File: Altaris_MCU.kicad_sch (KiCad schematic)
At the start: 81 parts, among them J1 Screw_Terminal_01x02, J10 USB_C_Receptacle_USB2.0_16P, J11 Screw_Terminal_01x02, J2 Screw_Terminal_01x02, J3 Screw_Terminal_01x02, J4 Screw_Terminal_01x02, J5 Screw_Terminal_01x02, J6 Screw_Terminal_01x02, J7 Conn_01x08_Socket, J8 Screw_Terminal_01x02, J9 USB_C_Receptacle_USB2.0_16P, Q1 Q_NMOS, SW2 RESET1, SW3 BOOT1, U1 ESP32-S3-WROOM-1, U10 USBLC6-2SC6, U11 MAX31855KASA, U12 TPS62827DMQT, U13 USBLC6-2SC6, U15 CH340X, U2 MAX31855KASA, U3 TPS79333-EP, U4 ICM-20948, U5 TPS79318-EP, U6 SN74AVC4T774RSVR, U7 MAX31855KASA, U8 MAX31855KASA, U9 SN74AVC4T774RSVR

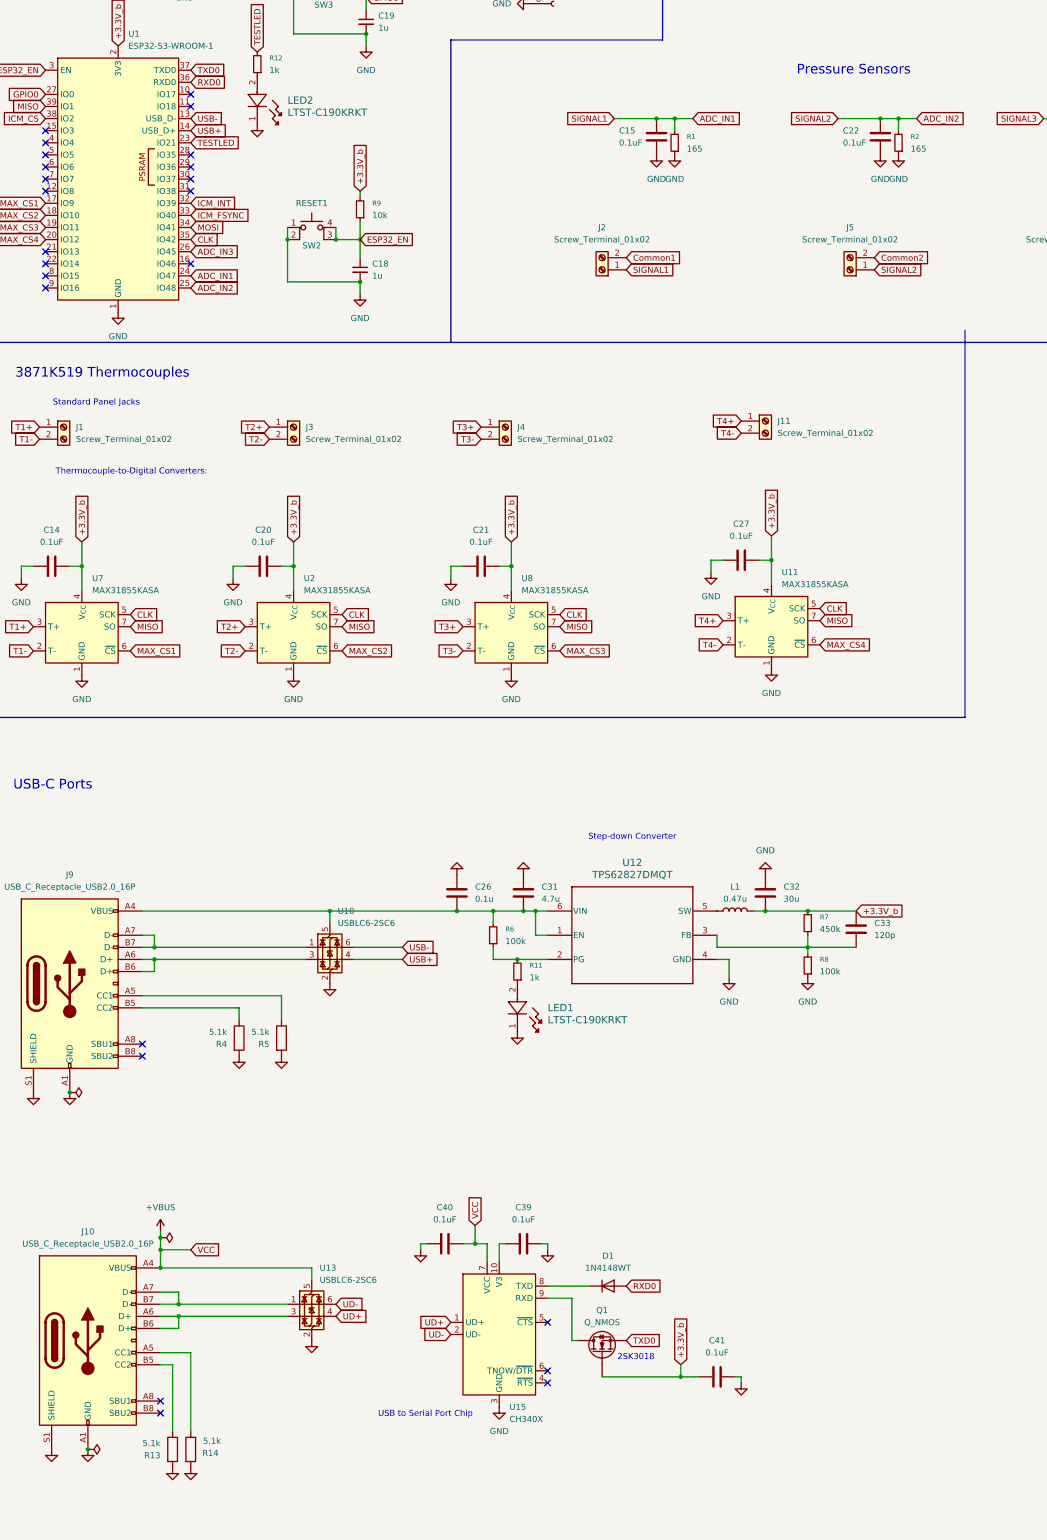
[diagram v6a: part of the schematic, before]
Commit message: Small changes to USB ports, ran ERC
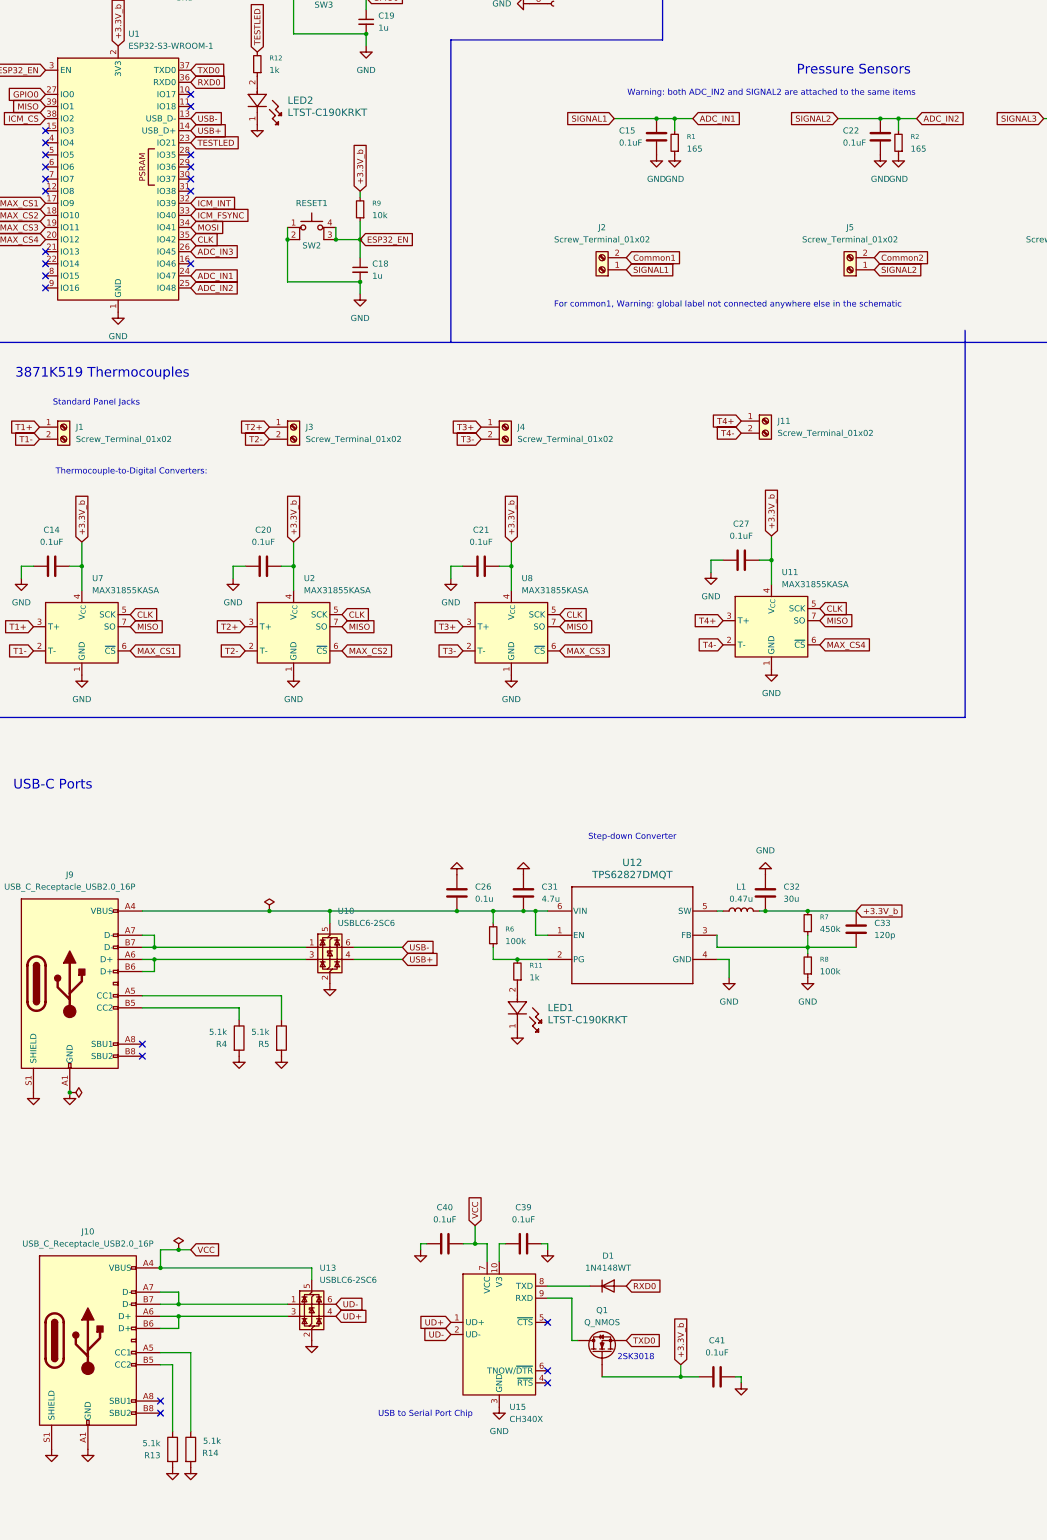
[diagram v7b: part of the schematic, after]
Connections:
- net +VBUS renamed VCC
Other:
- note added: "For common1, Warning: global label not connected anywhere else in the schematic"
- note added: "Warning: both ADC_IN2 and SIGNAL2 are attached to the same items"
- moved on the sheet: L1
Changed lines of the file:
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@@
 		)
 	)
+	(text "For common1, Warning: global label not connected anywhere else in the schematic"
+		(exclude_from_sim no)
+		(at 169.926 106.426 0)
+		(effects
+			(font
+				(size 1.27 1.27)
+			)
+		)
+	)
 	(text "Step-down Converter"
 		(exclude_from_sim no)
@@
 		)
 	)
+	(text "Warning: both ADC_IN2 and SIGNAL2 are attached to the same items"
+		(exclude_from_sim no)
+		(at 179.07 61.976 0)
+		(effects
+			(font
+				(size 1.27 1.27)
+			)
+		)
+	)
 	(text "WILL PROBOLY GET RID OF THIS LDO\n					   	    "
 		(exclude_from_sim no)
@@
 	)
 	(junction
-		(at 35.56 346.71)
-		(diameter 0)
-		(color 0 0 0 0)
-	)
-	(junction
 		(at 78.74 41.91)
 		(diameter 0)
@@
 	)
 	(junction
+		(at 73.66 233.68)
+		(diameter 0)
+		(color 0 0 0 0)
+	)
+	(junction
 		(at 120.65 233.68)
 		(diameter 0)
@@
 	)
 	(junction
+		(at 54.61 304.8)
+		(diameter 0)
+		(color 0 0 0 0)
+	)
+	(junction
 		(at 542.29 140.97)
 		(diameter 0)
@@
 	)
 	(junction
-		(at 50.8 302.26)
-		(diameter 0)
-		(color 0 0 0 0)
-	)
-	(junction
 		(at 350.52 44.45)
 		(diameter 0)
@@
 	)
 	(junction
-		(at 50.8 304.8)
-		(diameter 0)
-		(color 0 0 0 0)
-	)
-	(junction
 		(at 186.69 233.68)
 		(diameter 0)
@@
 	(wire
 		(pts
-			(xy 50.8 302.26) (xy 50.8 304.8)
-		)
-		(stroke
-			(width 0)
-			(type default)
-		)
-	)
-	(wire
-		(pts
 			(xy 176.53 160.02) (xy 179.07 160.02)
 		)
@@
 	(wire
 		(pts
+			(xy 54.61 304.8) (xy 50.8 304.8)
+		)
+		(stroke
+			(width 0)
+			(type default)
+		)
+	)
+	(wire
+		(pts
 			(xy 170.18 243.84) (xy 170.18 247.65)
 		)
@@
 	(wire
 		(pts
+			(xy 168.91 233.68) (xy 167.64 233.68)
+		)
+		(stroke
+			(width 0)
+			(type default)
+		)
+	)
+	(wire
+		(pts
 			(xy 120.65 233.68) (xy 127 233.68)
 		)
@@
 	(wire
 		(pts
-			(xy 50.8 300.99) (xy 50.8 302.26)
-		)
-		(stroke
-			(width 0)
-			(type default)
-		)
-	)
-	(wire
-		(pts
 			(xy 474.98 114.3) (xy 474.98 130.81)
 		)
@@
 	(wire
 		(pts
-			(xy 46.99 233.68) (xy 86.36 233.68)
+			(xy 46.99 233.68) (xy 73.66 233.68)
 		)
 		(stroke
@@
 	(wire
 		(pts
-			(xy 57.15 304.8) (xy 50.8 304.8)
+			(xy 57.15 304.8) (xy 54.61 304.8)
 		)
 		(stroke
@@
 	(wire
 		(pts
+			(xy 73.66 233.68) (xy 86.36 233.68)
+		)
+		(stroke
+			(width 0)
+			(type default)
+		)
+	)
+	(wire
+		(pts
 			(xy 236.22 67.31) (xy 245.11 67.31)
 		)
@@
 	(wire
 		(pts
-			(xy 175.26 233.68) (xy 177.8 233.68)
+			(xy 176.53 233.68) (xy 177.8 233.68)
 		)
 		(stroke
@@
 	(symbol
 		(lib_id "power:PWR_FLAG")
-		(at 50.8 302.26 270)
+		(at 54.61 304.8 0)
 		(unit 1)
 		(exclude_from_sim no)
@@
 		(fields_autoplaced yes)
 		(property "Reference" "#FLG07"
-			(at 52.705 302.26 0)
+			(at 54.61 302.895 0)
 			(effects
 				(font
@@
 		)
 		(property "Value" "PWR_FLAG"
-			(at 55.88 302.26 0)
+			(at 54.61 299.72 0)
 			(effects
 				(font
@@
 		)
 		(property "Footprint" ""
-			(at 50.8 302.26 0)
+			(at 54.61 304.8 0)
 			(effects
 				(font
@@
 		)
 		(property "Datasheet" "~"
-			(at 50.8 302.26 0)
+			(at 54.61 304.8 0)
 			(effects
 				(font
@@
 		)
 		(property "Description" "Special symbol for telling ERC where power comes from"
-			(at 50.8 302.26 0)
+			(at 54.61 304.8 0)
 			(effects
 				(font
@@
 	)
 	(symbol
+		(lib_id "power:PWR_FLAG")
+		(at 73.66 233.68 0)
+		(unit 1)
+		(exclude_from_sim no)
+		(in_bom yes)
+		(on_board yes)
+		(dnp no)
+		(fields_autoplaced yes)
+		(property "Reference" "#FLG02"
+			(at 73.66 231.775 0)
+			(effects
+				(font
+					(size 1.27 1.27)
+				)
+				(hide yes)
+			)
+		)
+		(property "Value" "PWR_FLAG"
+			(at 73.66 228.6 0)
+			(effects
+				(font
+					(size 1.27 1.27)
+				)
+				(hide yes)
+			)
+		)
+		(property "Footprint" ""
+			(at 73.66 233.68 0)
+			(effects
+				(font
+					(size 1.27 1.27)
+				)
+				(hide yes)
+			)
+		)
+		(property "Datasheet" "~"
+			(at 73.66 233.68 0)
+			(effects
+				(font
+					(size 1.27 1.27)
+				)
+				(hide yes)
+			)
+		)
+		(property "Description" "Special symbol for telling ERC where power comes from"
+			(at 73.66 233.68 0)
+			(effects
+				(font
+					(size 1.27 1.27)
+				)
+				(hide yes)
+			)
+		)
+		(pin "1"
+		)
+		(instances
+			(project "Altaris_MCU"
+				(path "/21889916-6808-460c-a148-21d1f170ea7e"
+					(reference "#FLG02")
+					(unit 1)
+				)
+			)
+		)
+	)
+	(symbol
 		(lib_id "power:GND")
 		(at 518.16 71.12 270)
@@
 	)
 	(symbol
-		(lib_id "power:PWR_FLAG")
-		(at 35.56 346.71 270)
-		(unit 1)
-		(exclude_from_sim no)
-		(in_bom yes)
-		(on_board yes)
-		(dnp no)
-		(fields_autoplaced yes)
-		(property "Reference" "#FLG01"
-			(at 37.465 346.71 0)
-			(effects
-				(font
-					(size 1.27 1.27)
-				)
-				(hide yes)
-			)
-		)
-		(property "Value" "PWR_FLAG"
-			(at 40.64 346.71 0)
-			(effects
-				(font
-					(size 1.27 1.27)
-				)
-				(hide yes)
-			)
-		)
-		(property "Footprint" ""
-			(at 35.56 346.71 0)
-			(effects
-				(font
-					(size 1.27 1.27)
-				)
-				(hide yes)
-			)
-		)
-		(property "Datasheet" "~"
-			(at 35.56 346.71 0)
-			(effects
-				(font
-					(size 1.27 1.27)
-				)
-				(hide yes)
-			)
-		)
-		(property "Description" "Special symbol for telling ERC where power comes from"
-			(at 35.56 346.71 0)
-			(effects
-				(font
-					(size 1.27 1.27)
-				)
-				(hide yes)
-			)
-		)
-		(pin "1"
-		)
-		(instances
-			(project "Altaris_MCU"
-				(path "/21889916-6808-460c-a148-21d1f170ea7e"
-					(reference "#FLG01")
-					(unit 1)
-				)
-			)
-		)
-	)
-	(symbol
 		(lib_id "power:GND")
 		(at 377.19 36.83 180)
@@
 	)
 	(symbol
-		(lib_id "power:VBUS")
-		(at 50.8 300.99 0)
-		(unit 1)
-		(exclude_from_sim no)
-		(in_bom yes)
-		(on_board yes)
-		(dnp no)
-		(fields_autoplaced yes)
-		(property "Reference" "#PWR077"
-			(at 50.8 304.8 0)
-			(effects
-				(font
-					(size 1.27 1.27)
-				)
-				(hide yes)
-			)
-		)
-		(property "Value" "+VBUS"
-			(at 50.8 295.91 0)
-			(effects
-				(font
-					(size 1.27 1.27)
-				)
-			)
-		)
-		(property "Footprint" ""
-			(at 50.8 300.99 0)
-			(effects
-				(font
-					(size 1.27 1.27)
-				)
-				(hide yes)
-			)
-		)
-		(property "Datasheet" ""
-			(at 50.8 300.99 0)
-			(effects
-				(font
-					(size 1.27 1.27)
-				)
-				(hide yes)
-			)
-		)
-		(property "Description" "Power symbol creates a global label with name \"VBUS\""
-			(at 50.8 300.99 0)
-			(effects
-				(font
-					(size 1.27 1.27)
-				)
-				(hide yes)
-			)
-		)
-		(pin "1"
-		)
-		(instances
-			(project "Altaris_MCU"
-				(path "/21889916-6808-460c-a148-21d1f170ea7e"
-					(reference "#PWR077")
-					(unit 1)
-				)
-			)
-		)
-	)
-	(symbol
 		(lib_id "power:GND")
 		(at 111.76 163.83 0)
@@
 	(symbol
 		(lib_id "Device:L")
-		(at 171.45 233.68 90)
+		(at 172.72 233.68 90)
 		(unit 1)
 		(exclude_from_sim no)
@@
 		(fields_autoplaced yes)
 		(property "Reference" "L1"
-			(at 171.45 228.6 90)
+			(at 172.72 228.6 90)
 			(effects
 				(font
@@
 		)
 		(property "Value" "0.47u"
-			(at 171.45 231.14 90)
+			(at 172.72 231.14 90)
 			(effects
 				(font
@@
 		)
 		(property "Footprint" "MyFootprints:IND_XFL4015_COC"
-			(at 171.45 233.68 0)
+			(at 172.72 233.68 0)
 			(effects
 				(font
@@
 		)
 		(property "Datasheet" "~"
-			(at 171.45 233.68 0)
+			(at 172.72 233.68 0)
 			(effects
 				(font
@@
 		)
 		(property "Description" "Inductor"
-			(at 171.45 233.68 0)
+			(at 172.72 233.68 0)
 			(effects
 				(font

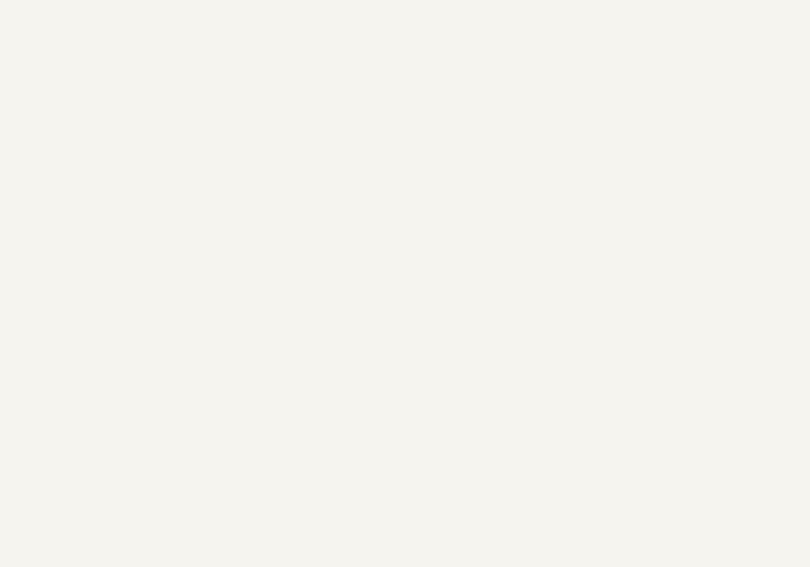
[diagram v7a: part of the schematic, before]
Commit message: added stitching vias, added power screw terminals
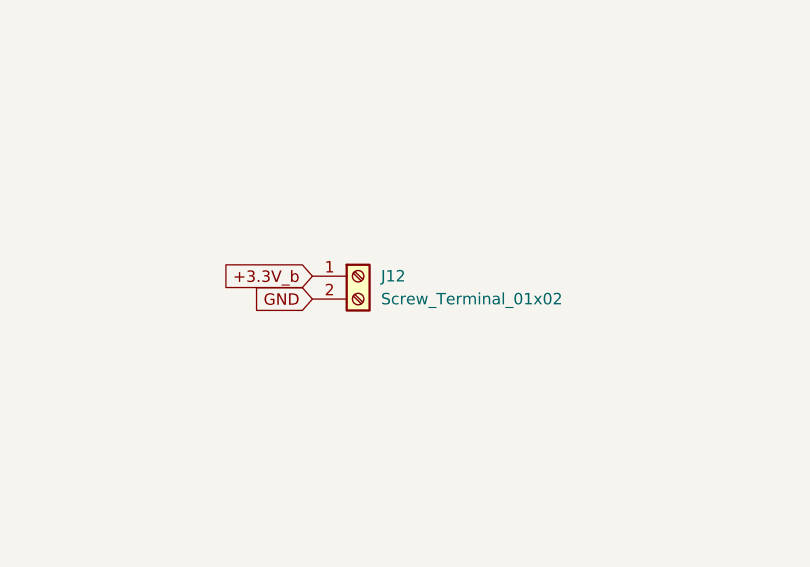
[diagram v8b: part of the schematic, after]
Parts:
- added J12: Screw_Terminal_01x02, TerminalBlock:TerminalBlock_MaiXu_MX126-5.0-02P_1x02_P5.00mm, symbol Connector:Screw_Terminal_01x02
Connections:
- net +3.3V_b: now also J12.1 (Pin_1)
- net GND: now also J12.2 (Pin_2)
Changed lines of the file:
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@@
 		)
 	)
+	(global_label "GND"
+		(shape input)
+		(at 271.78 149.86 180)
+		(fields_autoplaced yes)
+		(effects
+			(font
+				(size 1.27 1.27)
+			)
+			(justify right)
+		)
+		(property "Intersheetrefs" "${INTERSHEET_REFS}"
+			(at 264.9243 149.86 0)
+			(effects
+				(font
+					(size 1.27 1.27)
+				)
+				(justify right)
+				(hide yes)
+			)
+		)
+	)
 	(global_label "SIGNAL1"
 		(shape input)
@@
 		)
 	)
+	(global_label "+3.3V_b"
+		(shape input)
+		(at 271.78 147.32 180)
+		(fields_autoplaced yes)
+		(effects
+			(font
+				(size 1.27 1.27)
+			)
+			(justify right)
+		)
+		(property "Intersheetrefs" "${INTERSHEET_REFS}"
+			(at 260.9934 147.32 0)
+			(effects
+				(font
+					(size 1.27 1.27)
+				)
+				(justify right)
+				(hide yes)
+			)
+		)
+	)
 	(global_label "MAX_CS4"
 		(shape input)
@@
 					(unit 1)
 				)
+			)
+		)
+	)
+	(symbol
+		(lib_id "Connector:Screw_Terminal_01x02")
+		(at 276.86 147.32 0)
+		(unit 1)
+		(exclude_from_sim no)
+		(in_bom yes)
+		(on_board yes)
+		(dnp no)
+		(fields_autoplaced yes)
+		(property "Reference" "J12"
+			(at 279.4 147.3199 0)
+			(effects
+				(font
+					(size 1.27 1.27)
+				)
+				(justify left)
+			)
+		)
+		(property "Value" "Screw_Terminal_01x02"
+			(at 279.4 149.8599 0)
+			(effects
+				(font
+					(size 1.27 1.27)
+				)
+				(justify left)
+			)
+		)
+		(property "Footprint" "TerminalBlock:TerminalBlock_MaiXu_MX126-5.0-02P_1x02_P5.00mm"
+			(at 276.86 147.32 0)
+			(effects
+				(font
+					(size 1.27 1.27)
+				)
+				(hide yes)
+			)
+		)
+		(property "Datasheet" "~"
+			(at 276.86 147.32 0)
+			(effects
+				(font
+					(size 1.27 1.27)
+				)
+				(hide yes)
+			)
+		)
+		(property "Description" "Generic screw terminal, single row, 01x02, script generated (kicad-library-utils/schlib/autogen/connector/)"
+			(at 276.86 147.32 0)
+			(effects
+				(font
+					(size 1.27 1.27)
+				)
+				(hide yes)
+			)
+		)
+		(pin "1"
+		)
+		(pin "2"
+		)
+		(instances
+			(project "Altaris_MCU"
+				(path "/21889916-6808-460c-a148-21d1f170ea7e"
+					(reference "J12")
+					(unit 1)
+				)
